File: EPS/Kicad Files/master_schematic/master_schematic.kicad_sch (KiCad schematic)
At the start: 0 parts

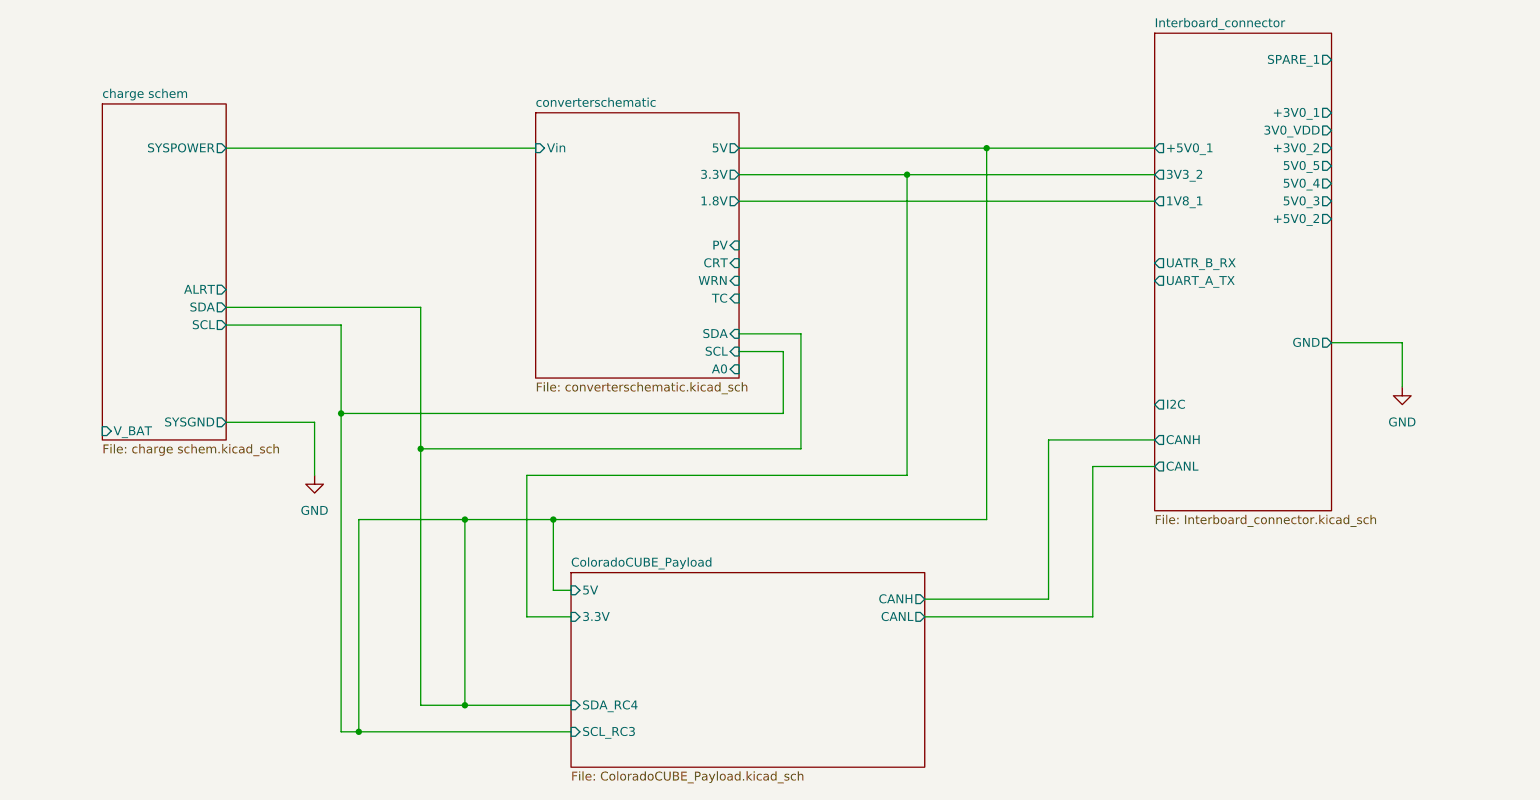
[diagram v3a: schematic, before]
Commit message: revised EPS schematics
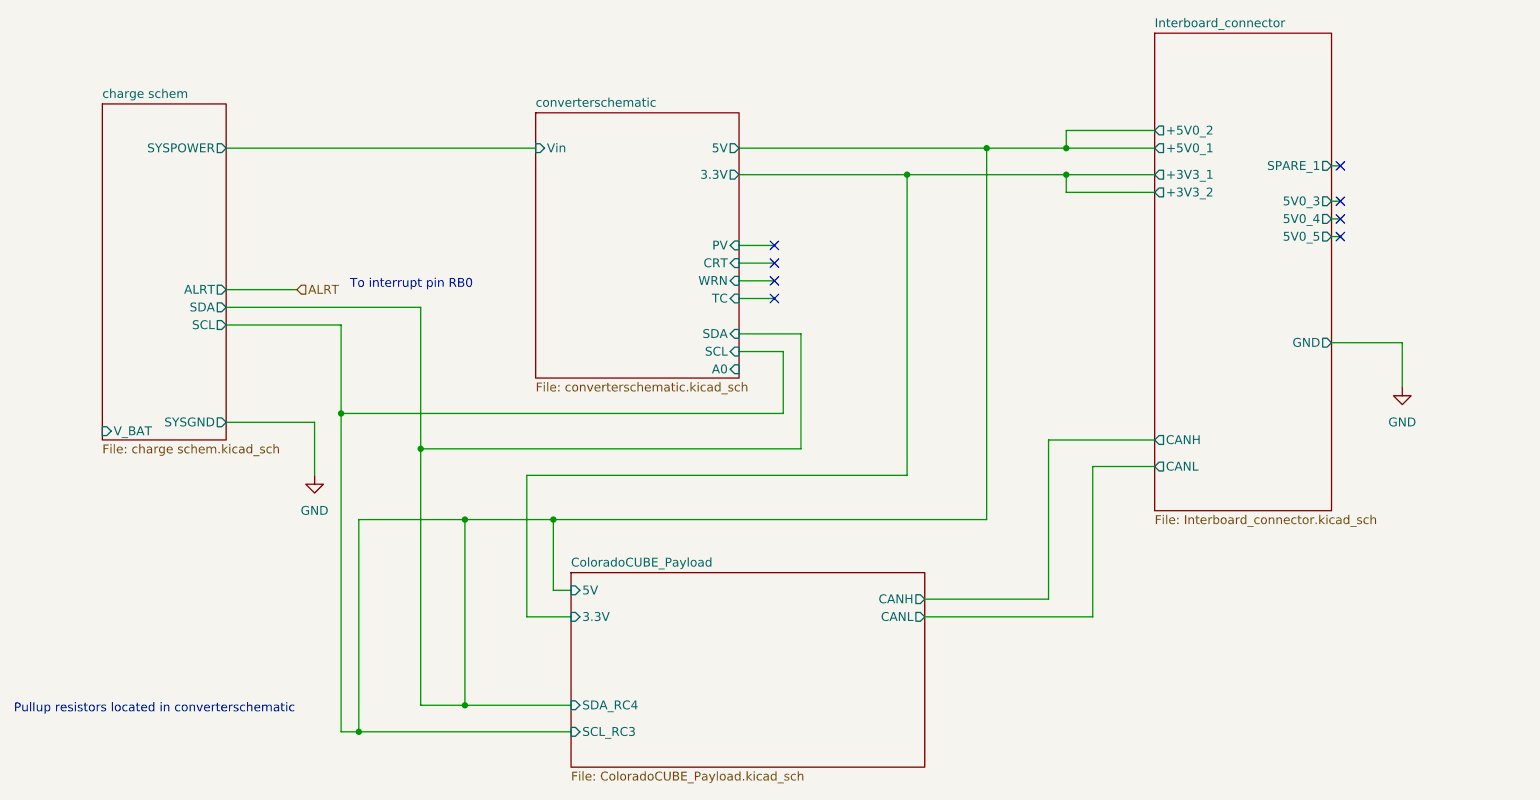
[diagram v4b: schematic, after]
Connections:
- no-connect marks 0 -> 8
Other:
- sheet Interboard_connector ports: added +3V3_1, +3V3_2; removed +3V0_1, +3V0_2, 1V8_1, 3V0_VDD, 3V3_2, I2C, UART_A_TX, UATR_B_RX
- sheet converterschematic ports: added none; removed 1.8V
- note added: "Pullup resistors located in converterschematic"
- note added: "To interrupt pin RB0"
- company: (none) -> MSU Denver Senior Project
- title: (none) -> ColoradoCUBE: EPS Subsystem

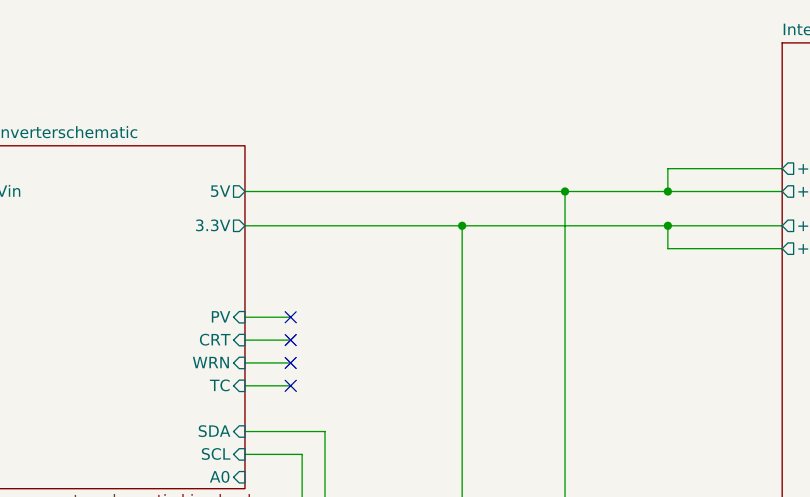
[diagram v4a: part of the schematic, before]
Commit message: master schematic/pcb update
updates schematic with OVP and added OVP to the PCB layout
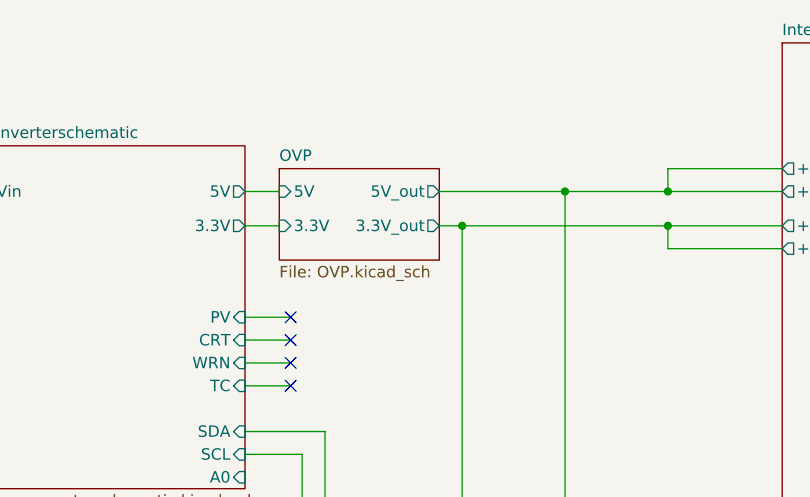
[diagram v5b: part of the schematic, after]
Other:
- added sheet OVP (OVP.kicad_sch)
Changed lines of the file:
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@@
   (junction (at 111.76 147.32) (diameter 0) (color 0 0 0 0)
   )
+  (junction (at 93.98 105.41) (diameter 0) (color 0 0 0 0)
+  )
+  (junction (at 111.76 120.65) (diameter 0) (color 0 0 0 0)
+  )
+  (junction (at 96.52 151.13) (diameter 0) (color 0 0 0 0)
+  )
+  (junction (at 186.69 67.31) (diameter 0) (color 0 0 0 0)
+  )
+  (junction (at 198.12 71.12) (diameter 0) (color 0 0 0 0)
+  )
   (junction (at 175.26 71.12) (diameter 0) (color 0 0 0 0)
   )
-  (junction (at 93.98 105.41) (diameter 0) (color 0 0 0 0)
-  )
-  (junction (at 111.76 120.65) (diameter 0) (color 0 0 0 0)
-  )
-  (junction (at 96.52 151.13) (diameter 0) (color 0 0 0 0)
-  )
-  (junction (at 198.12 71.12) (diameter 0) (color 0 0 0 0)
-  )
   (junction (at 198.12 67.31) (diameter 0) (color 0 0 0 0)
-  )
-  (junction (at 186.69 67.31) (diameter 0) (color 0 0 0 0)
   )
   (no_connect (at 156.21 81.28))
@@
     (stroke (width 0) (type default) (color 0 0 0 0))
   )
-  (wire (pts (xy 151.13 67.31) (xy 186.69 67.31))
-    (stroke (width 0) (type default) (color 0 0 0 0))
-  )
   (wire (pts (xy 93.98 105.41) (xy 93.98 151.13))
     (stroke (width 0) (type default) (color 0 0 0 0))
@@
     (stroke (width 0) (type default) (color 0 0 0 0))
   )
+  (wire (pts (xy 172.72 71.12) (xy 175.26 71.12))
+    (stroke (width 0) (type default) (color 0 0 0 0))
+  )
   (wire (pts (xy 105.41 110.49) (xy 105.41 147.32))
     (stroke (width 0) (type default) (color 0 0 0 0))
@@
     (stroke (width 0) (type default) (color 0 0 0 0))
   )
+  (wire (pts (xy 151.13 71.12) (xy 154.94 71.12))
+    (stroke (width 0) (type default) (color 0 0 0 0))
+  )
   (wire (pts (xy 151.13 93.98) (xy 160.02 93.98))
     (stroke (width 0) (type default) (color 0 0 0 0))
@@
     (stroke (width 0) (type default) (color 0 0 0 0))
   )
-  (wire (pts (xy 175.26 71.12) (xy 151.13 71.12))
-    (stroke (width 0) (type default) (color 0 0 0 0))
-  )
   (wire (pts (xy 151.13 88.9) (xy 156.21 88.9))
     (stroke (width 0) (type default) (color 0 0 0 0))
@@
     (stroke (width 0) (type default) (color 0 0 0 0))
   )
+  (wire (pts (xy 172.72 67.31) (xy 186.69 67.31))
+    (stroke (width 0) (type default) (color 0 0 0 0))
+  )
   (wire (pts (xy 105.41 90.17) (xy 105.41 110.49))
     (stroke (width 0) (type default) (color 0 0 0 0))
@@
   )
   (wire (pts (xy 105.41 110.49) (xy 160.02 110.49))
+    (stroke (width 0) (type default) (color 0 0 0 0))
+  )
+  (wire (pts (xy 151.13 67.31) (xy 154.94 67.31))
     (stroke (width 0) (type default) (color 0 0 0 0))
   )
@@
     )
   )
+  (sheet (at 154.94 64.77) (size 17.78 10.16) (fields_autoplaced)
+    (stroke (width 0.1524) (type solid) (color 0 0 0 0))
+    (fill (color 0 0 0 0.0000))
+    (property "Sheet name" "OVP" (id 0) (at 154.94 64.0584 0)
+      (effects (font (size 1.27 1.27)) (justify left bottom))
+    )
+    (property "Sheet file" "OVP.kicad_sch" (id 1) (at 154.94 75.5146 0)
+      (effects (font (size 1.27 1.27)) (justify left top))
+    )
+    (pin "5V" input (at 154.94 67.31 180)
+      (effects (font (size 1.27 1.27)) (justify left))
+    )
+    (pin "3.3V" input (at 154.94 71.12 180)
+      (effects (font (size 1.27 1.27)) (justify left))
+    )
+    (pin "5V_out" output (at 172.72 67.31 0)
+      (effects (font (size 1.27 1.27)) (justify right))
+    )
+    (pin "3.3V_out" output (at 172.72 71.12 0)
+      (effects (font (size 1.27 1.27)) (justify right))
+    )
+  )
   (sheet_instances
     (path "/" (page "1"))
     (path "/59a4dc33-016c-4cea-b648-6fe1c8836f68" (page "2"))
     (path "/26a06af6-a463-4c0b-bc99-b7ef2964e4cd" (page "3"))
-    (path "/3a06e4e0-634b-426a-a0ab-d37016f35ddc/4e16fedc-a38b-401e-a5de-03896de0e471" (page "#"))
     (path "/009ce997-1584-43ca-93af-c5bcacd4d4e9" (page "5"))
     (path "/3a06e4e0-634b-426a-a0ab-d37016f35ddc" (page "6"))
+    (path "/68881549-1588-438c-abf8-f6f2c2b6b5a2" (page "8"))
+    (path "/3a06e4e0-634b-426a-a0ab-d37016f35ddc/4e16fedc-a38b-401e-a5de-03896de0e471" (page "#"))
     (path "/3a06e4e0-634b-426a-a0ab-d37016f35ddc/a47b42ae-0735-4637-85df-404ec278273a" (page "#"))
   )
@@
       (reference "#PWR0124") (unit 1) (value "GND") (footprint "")
     )
+    (path "/68881549-1588-438c-abf8-f6f2c2b6b5a2/61c56995-1f38-4247-871c-79e0c9e5ef8c"
+      (reference "#PWR?") (unit 1) (value "GND") (footprint "")
+    )
+    (path "/68881549-1588-438c-abf8-f6f2c2b6b5a2/d43e0384-fb1f-44ed-9afb-6122265a09ac"
+      (reference "#PWR?") (unit 1) (value "GND") (footprint "")
+    )
     (path "/3a06e4e0-634b-426a-a0ab-d37016f35ddc/a47b42ae-0735-4637-85df-404ec278273a/6ae01795-5ad6-47dc-b699-07dfe82cc4e1"
       (reference "C1") (unit 1) (value "4.7nF") (footprint "Capacitor_SMD:C_0603_1608Metric_Pad1.08x0.95mm_HandSolder")
@@
       (reference "C11") (unit 1) (value "0.47uF") (footprint "Capacitor_SMD:C_0603_1608Metric")
     )
+    (path "/68881549-1588-438c-abf8-f6f2c2b6b5a2/4c8bce28-a190-4be2-ac35-9540cf27f8ae"
+      (reference "CR?") (unit 1) (value "BZX884B5V1L-HG3-08") (footprint "CR_1L-HG3-08_VIS")
+    )
     (path "/3a06e4e0-634b-426a-a0ab-d37016f35ddc/4bff1f15-0047-457d-ac78-28e14a16e610"
       (reference "D1") (unit 1) (value "DIODE") (footprint "Diode_SMD:D_0805_2012Metric_Pad1.15x1.40mm_HandSolder")
@@
       (reference "D6") (unit 1) (value "YELLOW") (footprint "LED_SMD:LED_0603_1608Metric_Pad1.05x0.95mm_HandSolder")
     )
+    (path "/68881549-1588-438c-abf8-f6f2c2b6b5a2/be4e4217-76b2-49d6-ac01-d4e643194de5"
+      (reference "D?") (unit 1) (value "PD3Z284C3V6-7") (footprint "PowerDI323_DIO")
+    )
     (path "/009ce997-1584-43ca-93af-c5bcacd4d4e9/ba9a4ebf-5eec-4d42-b8b4-9df72964a241"
       (reference "J1") (unit 1) (value "Conn_02x20_Odd_Even") (footprint "Connector_PinHeader_2.54mm:PinHeader_2x20_P2.54mm_Vertical")
@@
       (reference "L1") (unit 1) (value ".47uH") (footprint "Inductor_SMD:L_1008_2520Metric")
     )
+    (path "/68881549-1588-438c-abf8-f6f2c2b6b5a2/e41ab162-a2fa-44a9-91bd-bd7c3ab2148c"
+      (reference "Q1") (unit 1) (value "FZT688BTA") (footprint "Package_TO_SOT_THT:TO-39-3")
+    )
+    (path "/68881549-1588-438c-abf8-f6f2c2b6b5a2/f968db49-d235-4124-9198-1a48098a8944"
+      (reference "Q2") (unit 1) (value "FZT688BTA") (footprint "Package_TO_SOT_THT:TO-39-3")
+    )
     (path "/59a4dc33-016c-4cea-b648-6fe1c8836f68/15d23d40-e1de-4a7e-8dae-2d49cf508cd4"
       (reference "R1") (unit 1) (value "PSF4NTEBL500F") (footprint "footprints:PSF4NTEBL500F")
@@
       (reference "R1") (unit 1) (value "60") (footprint "Resistor_SMD:R_0603_1608Metric_Pad0.98x0.95mm_HandSolder")
     )
+    (path "/68881549-1588-438c-abf8-f6f2c2b6b5a2/f9214b32-7510-4f37-a128-f4dcd389433e"
+      (reference "R1") (unit 1) (value "1k") (footprint "")
+    )
     (path "/59a4dc33-016c-4cea-b648-6fe1c8836f68/0eedaf4c-41f6-48ba-98ff-d706984035d0"
       (reference "R2") (unit 1) (value "PSF4NTEBL500F") (footprint "footprints:PSF4NTEBL500F")
@@
       (reference "R2") (unit 1) (value "60") (footprint "Resistor_SMD:R_0603_1608Metric_Pad0.98x0.95mm_HandSolder")
     )
+    (path "/68881549-1588-438c-abf8-f6f2c2b6b5a2/6add0acd-edb2-4195-8baa-f2cc902d5d3d"
+      (reference "R2") (unit 1) (value "1k") (footprint "")
+    )
     (path "/26a06af6-a463-4c0b-bc99-b7ef2964e4cd/6cea931b-c40a-4033-85c0-bd8b53146a7a"
